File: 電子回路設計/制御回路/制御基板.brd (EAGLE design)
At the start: 64 x 36 mm, 19 parts, among them IC1 ATMEGA2560-16AU, Q1 HUSG-16.000-20

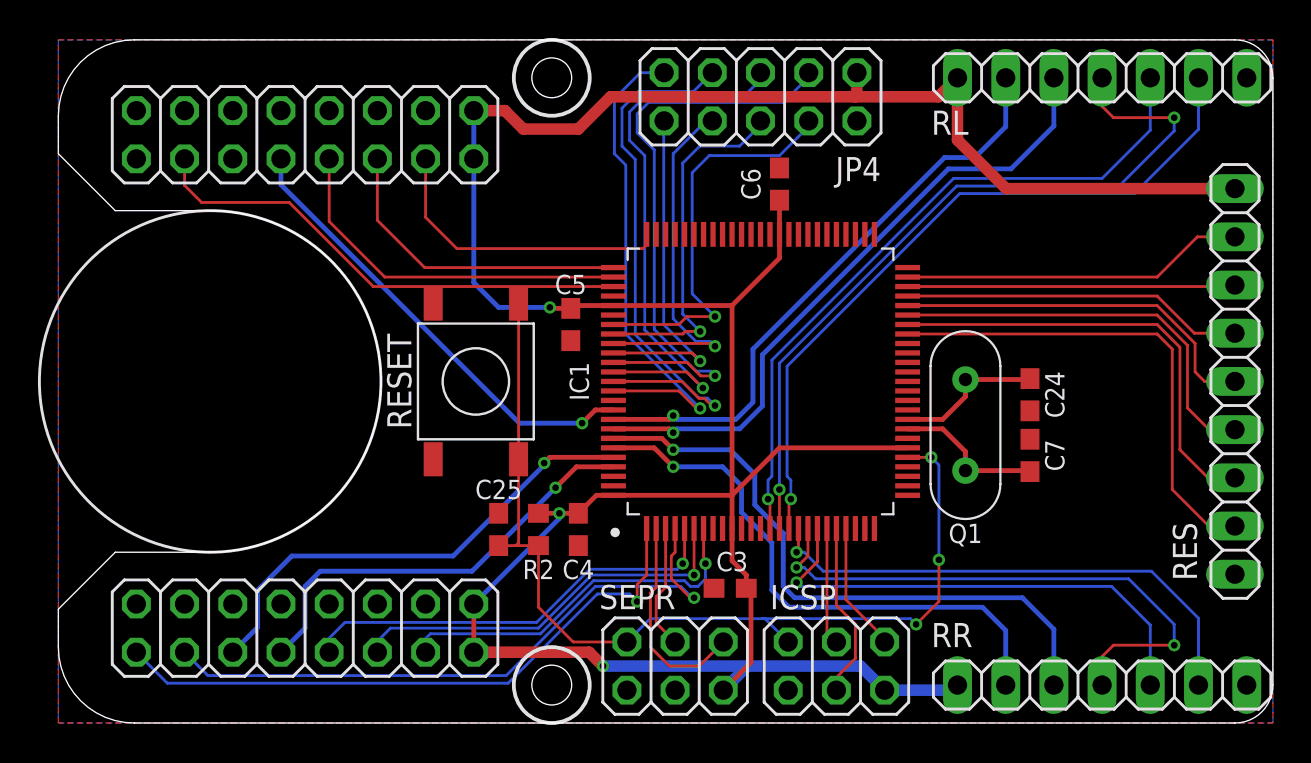
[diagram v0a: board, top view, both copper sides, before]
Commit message: fix : CB fix error
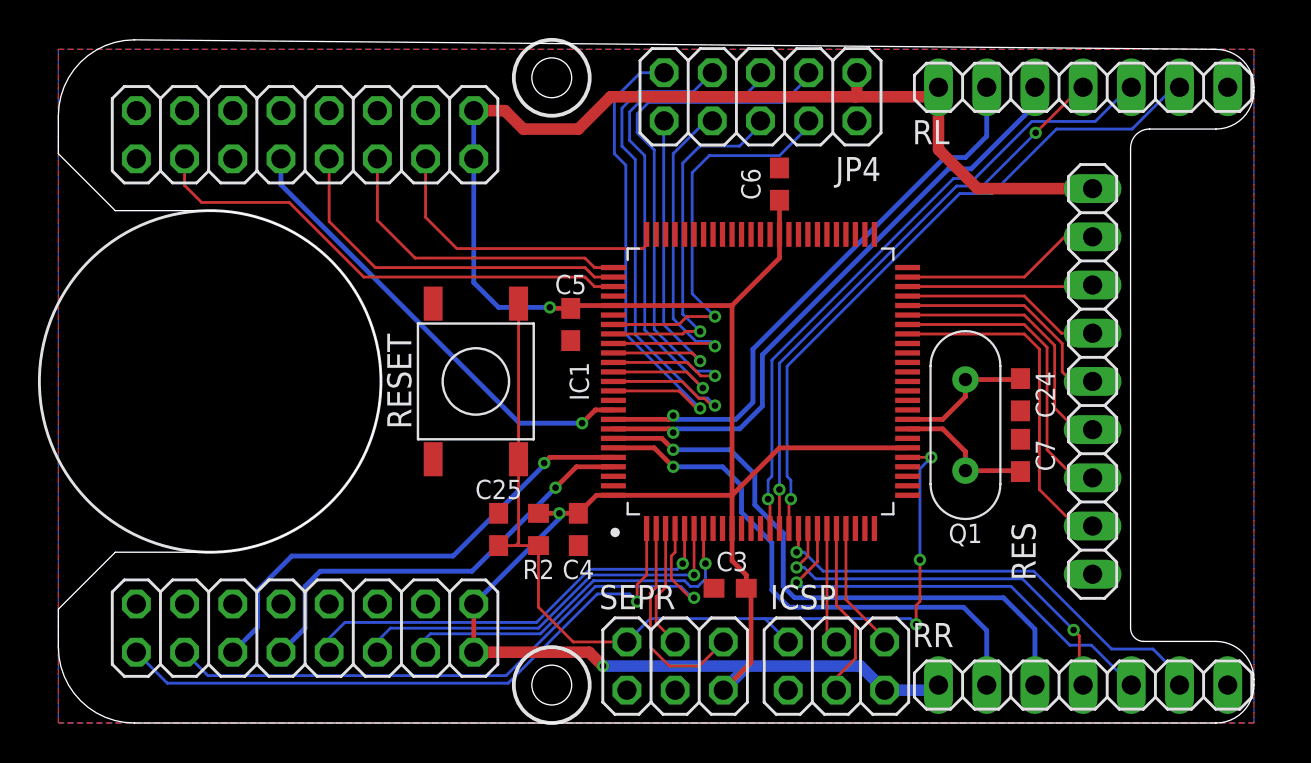
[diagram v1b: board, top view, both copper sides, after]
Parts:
- moved RES 7.50 mm to (46.5, 0.00)
- moved RL 1.12 mm to (46.0, 15.5)
- moved RR 1.00 mm to (46.0, -16.0)
- moved C24 0.50 mm to (42.7, -0.70)
- moved C7 0.50 mm to (42.7, -3.90)
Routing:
- net RL_PWM: track 40.8 -> 30.9 mm
- net +5V: track 158.5 -> 149.6 mm
- net RR_PWM: track 30.1 -> 21.4 mm
- net N$8: track 17.3 -> 9.78 mm
- net N$9: track 18.1 -> 10.6 mm
- net N$7: track 18.1 -> 10.6 mm
- net N$6: track 19.8 -> 12.3 mm
- net N$5: track 21.7 -> 14.2 mm
- net N$4: track 23.8 -> 16.3 mm
- net N$1: track 25.8 -> 18.3 mm
- net RR_EN: track 26.0 -> 23.2 mm
- net RL_EN: track 36.7 -> 33.9 mm
- net RL_DIR: track 38.2 -> 35.4 mm
- net RR_DIR: track 27.4 -> 24.7 mm
- net RL_IS2: track 34.1 -> 32.0 mm
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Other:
- board size 64 x 36 mm -> 63 x 36 mm

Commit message: fix : cam data
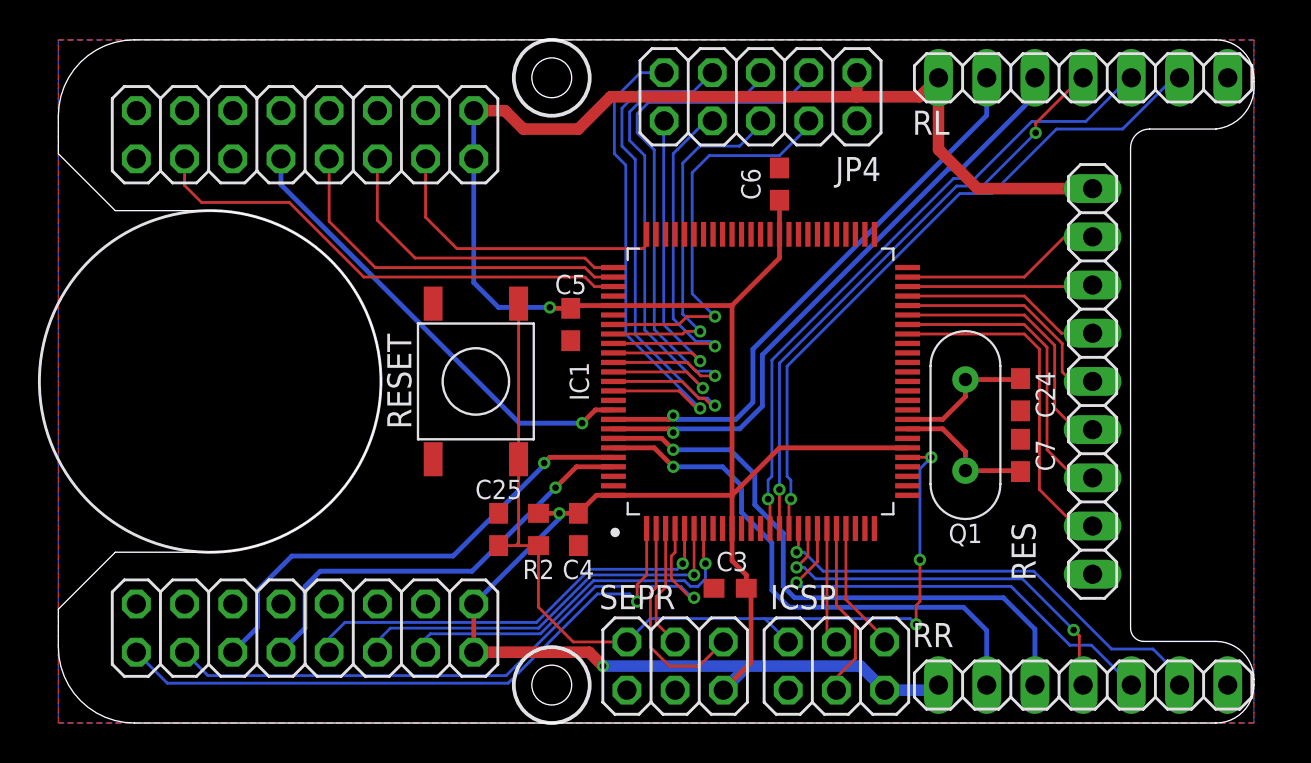
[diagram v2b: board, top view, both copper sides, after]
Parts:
- moved RL 0.50 mm to (46.0, 16.0)
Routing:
- net +5V: track 149.6 -> 150.3 mm
- net RL_PWM: track 30.9 -> 31.4 mm
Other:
- outline, holes or cut-outs redrawn
- board text added: "C24"
- board text added: "C25"
- board text added: "C3"
- board text added: "C4"
- board text added: "C5"
- board text added: "C6"
- board text added: "C7"
- board text added: "IC1"
- board text added: "ICSP"
- board text added: "JP4"
- board text added: "Q1"
- board text added: "R2"
- board text added: "RES"
- board text added: "RESET"
- board text added: "RL"
- board text added: "RR"
- board text added: "SEPR"
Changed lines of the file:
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@@
 <setting verticaltext="up"/>
 </settings>
-<grid distance="0.1" unitdist="mm" unit="mm" style="lines" multiple="1" display="yes" altdistance="5" altunitdist="mil" altunit="mil"/>
+<grid distance="0.5" unitdist="mm" unit="mm" style="lines" multiple="1" display="yes" altdistance="5" altunitdist="mil" altunit="mil"/>
 <layers>
 <layer number="1" name="Top" color="4" fill="1" visible="yes" active="yes"/>
@@
 <layer number="123" name="tTestmark" color="7" fill="1" visible="yes" active="yes"/>
 <layer number="124" name="bTestmark" color="7" fill="1" visible="yes" active="yes"/>
-<layer number="125" name="_tNames" color="7" fill="1" visible="yes" active="yes"/>
+<layer number="125" name="_tNames" color="14" fill="1" visible="yes" active="yes"/>
 <layer number="126" name="_bNames" color="7" fill="1" visible="yes" active="yes"/>
 <layer number="127" name="_tValues" color="7" fill="1" visible="yes" active="yes"/>
@@
 <plain>
 <wire x1="53" y1="-18" x2="-4" y2="-18" width="0" layer="20"/>
-<wire x1="-4" y1="18" x2="53" y2="17.5" width="0" layer="20"/>
-<wire x1="53" y1="17.5" x2="55" y2="15.5" width="0" layer="20" curve="-90"/>
+<wire x1="-4" y1="18" x2="53" y2="18" width="0" layer="20"/>
+<wire x1="53" y1="18" x2="55" y2="16" width="0" layer="20" curve="-90"/>
 <wire x1="55" y1="-16" x2="53" y2="-18" width="0" layer="20" curve="-90"/>
 <wire x1="-4" y1="-18" x2="-8" y2="-14" width="0" layer="20" curve="-90"/>
@@
 <wire x1="55" y1="-15.7" x2="55" y2="-16" width="0" layer="20"/>
 <wire x1="49.5" y1="13.3" x2="53" y2="13.3" width="0" layer="20"/>
-<wire x1="53" y1="13.3" x2="55" y2="15.3" width="0" layer="20" curve="90"/>
-<wire x1="55" y1="15.3" x2="55" y2="15.5" width="0" layer="20"/>
+<wire x1="53" y1="13.3" x2="55" y2="15.8" width="0" layer="20" curve="90"/>
+<wire x1="55" y1="15.8" x2="55" y2="16" width="0" layer="20"/>
+<text x="27.499996875" y="-10.00000625" size="1.016" layer="125" align="bottom-center">C3</text>
+<text x="19.4000125" y="-9.40000625" size="1.016" layer="125" rot="R180" align="bottom-center">C4</text>
+<text x="18.9999875" y="4.599990625" size="1.016" layer="125" align="bottom-center">C5</text>
+<text x="28.99999375" y="10.400003125" size="1.016" layer="125" rot="R90" align="bottom-center">C6</text>
+<text x="43.499990625" y="-3.89999375" size="1.016" layer="125" rot="R270" align="bottom-center">C7</text>
+<text x="43.499990625" y="-0.7" size="1.016" layer="125" rot="R270" align="bottom-center">C24</text>
+<text x="15.19999375" y="-6.1999875" size="1.016" layer="125" align="bottom-center">C25</text>
+<text x="19.959090625" y="0" size="1.016" layer="125" rot="R90" align="bottom-center">IC1</text>
+<text x="29.499990625" y="-12" size="1.27" layer="125" ratio="10">ICSP</text>
+<text x="35.34999375" y="11.824996875" size="1.27" layer="125" ratio="10" rot="R180">JP4</text>
+<text x="39.799996875" y="-7.500009375" size="1.016" layer="125" rot="R180" align="bottom-center">Q1</text>
+<text x="17.299990625" y="-9.40000625" size="1.016" layer="125" rot="R180" align="bottom-center">R2</text>
+<text x="43.499990625" y="-10.500003125" size="1.27" layer="125" ratio="10" rot="R90">RES</text>
+<text x="10.600003125" y="0" size="1.27" layer="125" rot="R90" align="bottom-center">RESET</text>
+<text x="37.000003125" y="13" size="1.27" layer="125" ratio="10">RL</text>
+<text x="37.000003125" y="-13.999996875" size="1.27" layer="125" ratio="10">RR</text>
+<text x="20.500009375" y="-12" size="1.27" layer="125" ratio="10">SEPR</text>
 </plain>
 <attributes>
@@
 <attribute name="VALUE" x="38.0409" y="0" size="1.27" layer="27" rot="R90" align="top-center"/>
 </element>
-<element name="RL" library="pinhead" package="1X07" package3d_urn="urn:adsk.eagle:package:22477/2" value="" x="46" y="15.5" smashed="yes">
-<attribute name="NAME" x="37" y="12.5" size="1.27" layer="25" ratio="10"/>
-<attribute name="POPULARITY" value="0" x="46" y="15.5" size="1.778" layer="27" display="off"/>
-<attribute name="VALUE" x="37.11" y="12.325" size="1.27" layer="27"/>
+<element name="RL" library="pinhead" package="1X07" package3d_urn="urn:adsk.eagle:package:22477/2" value="" x="46" y="16" smashed="yes">
+<attribute name="NAME" x="37" y="13" size="1.27" layer="25" ratio="10"/>
+<attribute name="POPULARITY" value="0" x="46" y="16" size="1.778" layer="27" display="off"/>
+<attribute name="VALUE" x="37.11" y="12.825" size="1.27" layer="27"/>
 </element>
 <element name="RR" library="pinhead" package="1X07" package3d_urn="urn:adsk.eagle:package:22477/2" value="" x="46" y="-16" smashed="yes">
@@
 <polygon width="0.1524" layer="1">
 <vertex x="-8" y="-18"/>
-<vertex x="-8" y="17.5"/>
-<vertex x="55" y="17.5"/>
+<vertex x="-8" y="18"/>
+<vertex x="55" y="18"/>
 <vertex x="55" y="-18"/>
 </polygon>
 <polygon width="0.1524" layer="16">
 <vertex x="55" y="-18"/>
-<vertex x="55" y="17.5"/>
-<vertex x="-8" y="17.5"/>
+<vertex x="55" y="18"/>
+<vertex x="-8" y="18"/>
 <vertex x="-8" y="-18"/>
 </polygon>
@@
 <wire x1="15.53" y1="14.27" x2="16.5" y2="13.3" width="0.6096" layer="1"/>
 <wire x1="16.5" y1="13.3" x2="19.4" y2="13.3" width="0.6096" layer="1"/>
-<wire x1="37.88" y1="15" x2="38.38" y2="15.5" width="0.6096" layer="1"/>
-<wire x1="37.88" y1="15" x2="34" y2="15" width="0.6096" layer="1"/>
+<wire x1="37.38" y1="15" x2="38.38" y2="16" width="0.6096" layer="1"/>
+<wire x1="37.38" y1="15" x2="34.08" y2="15" width="0.6096" layer="1"/>
 <wire x1="34" y1="15" x2="21.1" y2="15" width="0.6096" layer="1"/>
 <wire x1="19.4" y1="13.3" x2="21.1" y2="15" width="0.6096" layer="1"/>
@@
 <contactref element="RES" pad="1"/>
 <wire x1="46.5" y1="10.16" x2="40.44" y2="10.16" width="0.6096" layer="1"/>
-<wire x1="38.38" y1="12.22" x2="38.38" y2="15.5" width="0.6096" layer="1"/>
+<wire x1="38.38" y1="12.22" x2="38.38" y2="16" width="0.6096" layer="1"/>
 <wire x1="40.44" y1="10.16" x2="38.38" y2="12.22" width="0.6096" layer="1"/>
 <contactref element="JP4" pad="1"/>
-<wire x1="34.08" y1="16.27" x2="34.08" y2="15.08" width="0.6" layer="1"/>
+<wire x1="34.08" y1="16.27" x2="34.08" y2="15" width="0.6" layer="1"/>
 <wire x1="34.08" y1="15.08" x2="34" y2="15" width="0.6" layer="1"/>
 </signal>
@@
 <via x="24.4" y="-1.8" extent="1-16" drill="0.35"/>
 <wire x1="24.4" y1="-1.8" x2="24.6" y2="-2" width="0.254" layer="16"/>
-<wire x1="40.92" y1="12.92" x2="40.92" y2="15.5" width="0.254" layer="16"/>
+<wire x1="40.92" y1="14.02" x2="40.92" y2="16" width="0.254" layer="16"/>
 <wire x1="24.6" y1="-2" x2="27.7" y2="-2" width="0.254" layer="16"/>
 <wire x1="27.7" y1="-2" x2="28.6" y2="-1.1" width="0.254" layer="16"/>
 <wire x1="28.6" y1="-1.1" x2="28.6" y2="1.7" width="0.254" layer="16"/>
-<wire x1="28.6" y1="1.7" x2="38.7" y2="11.8" width="0.254" layer="16"/>
-<wire x1="38.7" y1="11.8" x2="39.8" y2="11.8" width="0.254" layer="16"/>
-<wire x1="39.8" y1="11.8" x2="40.92" y2="12.92" width="0.254" layer="16"/>
+<wire x1="28.6" y1="1.7" x2="40.92" y2="14.02" width="0.254" layer="16"/>
 </signal>
 <signal name="RL_IS2">
@@
 <wire x1="27.9" y1="-2.5" x2="29.1" y2="-1.3" width="0.254" layer="16"/>
 <wire x1="29.1" y1="-1.3" x2="29.1" y2="1.4" width="0.254" layer="16"/>
-<wire x1="43.46" y1="14.56" x2="43.46" y2="15.5" width="0.254" layer="16"/>
+<wire x1="43.46" y1="15.06" x2="43.46" y2="16" width="0.254" layer="16"/>
 <wire x1="29.1" y1="1.4" x2="38.9" y2="11.2" width="0.254" layer="16"/>
-<wire x1="38.9" y1="11.2" x2="40.1" y2="11.2" width="0.254" layer="16"/>
-<wire x1="40.1" y1="11.2" x2="43.46" y2="14.56" width="0.254" layer="16"/>
+<wire x1="38.9" y1="11.2" x2="39.6" y2="11.2" width="0.254" layer="16"/>
+<wire x1="39.6" y1="11.2" x2="43.46" y2="15.06" width="0.254" layer="16"/>
 </signal>
 <signal name="A_EN">
@@
 <wire x1="43.5" y1="13.0971875" x2="40.7" y2="10.2971875" width="0.15" layer="16"/>
 <via x="43.5" y="13.1" extent="1-16" drill="0.35"/>
-<wire x1="43.5" y1="13.1" x2="46" y2="15.6" width="0.15" layer="1"/>
-<wire x1="46" y1="15.6" x2="46" y2="15.5" width="0.15" layer="1"/>
+<wire x1="46" y1="16.1" x2="43.5" y2="13.6" width="0.15" layer="1"/>
+<wire x1="43.5" y1="13.1" x2="43.5" y2="13.6" width="0.15" layer="1"/>
+<wire x1="46" y1="16.1" x2="46" y2="16" width="0.15" layer="1"/>
 </signal>
 <signal name="RL_DIR">
@@
 <wire x1="30.4" y1="-5" x2="30.4" y2="0.8" width="0.15" layer="16"/>
 <wire x1="39.5" y1="9.9" x2="41.2" y2="9.9" width="0.15" layer="16"/>
-<wire x1="51.08" y1="15.5" x2="50.78" y2="15.5" width="0.15" layer="16"/>
-<wire x1="50.78" y1="15.5" x2="48.58" y2="13.3" width="0.15" layer="16"/>
-<wire x1="48.58" y1="13.3" x2="44.6" y2="13.3" width="0.15" layer="16"/>
+<wire x1="51.08" y1="16" x2="50.78" y2="16" width="0.15" layer="16"/>
+<wire x1="50.78" y1="16" x2="48.08" y2="13.3" width="0.15" layer="16"/>
+<wire x1="48.08" y1="13.3" x2="44.6" y2="13.3" width="0.15" layer="16"/>
 <wire x1="44.6" y1="13.3" x2="41.2" y2="9.9" width="0.15" layer="16"/>
 </signal>
@@
 <wire x1="39.17095" y1="10.694375" x2="29.6" y2="1.123425" width="0.15" layer="16"/>
 <wire x1="29.6" y1="-5" x2="29.6" y2="1.123425" width="0.15" layer="16"/>
-<wire x1="48.54" y1="15.5" x2="48.44" y2="15.5" width="0.15" layer="16"/>
-<wire x1="48.44" y1="15.5" x2="46.64" y2="13.7" width="0.15" layer="16"/>
-<wire x1="46.64" y1="13.7" x2="43.3" y2="13.7" width="0.15" layer="16"/>
+<wire x1="48.54" y1="16" x2="48.44" y2="16" width="0.15" layer="16"/>
+<wire x1="48.44" y1="16" x2="46.14" y2="13.7" width="0.15" layer="16"/>
+<wire x1="46.14" y1="13.7" x2="43.3" y2="13.7" width="0.15" layer="16"/>
 <wire x1="43.3" y1="13.7" x2="40.294375" y2="10.694375" width="0.15" layer="16"/>
 <wire x1="40.294375" y1="10.694375" x2="39.17095" y2="10.694375" width="0.15" layer="16"/>
